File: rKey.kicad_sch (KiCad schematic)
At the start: 39 parts, among them IC1 BDX34C, J1 Conn_01x06, Q1 BC337, Q2 BC337, Q3 BC337, Q4 BC337, Q5 BC327, Q8 BC337, U1 TL084BCN, U2 LM7810_TO220

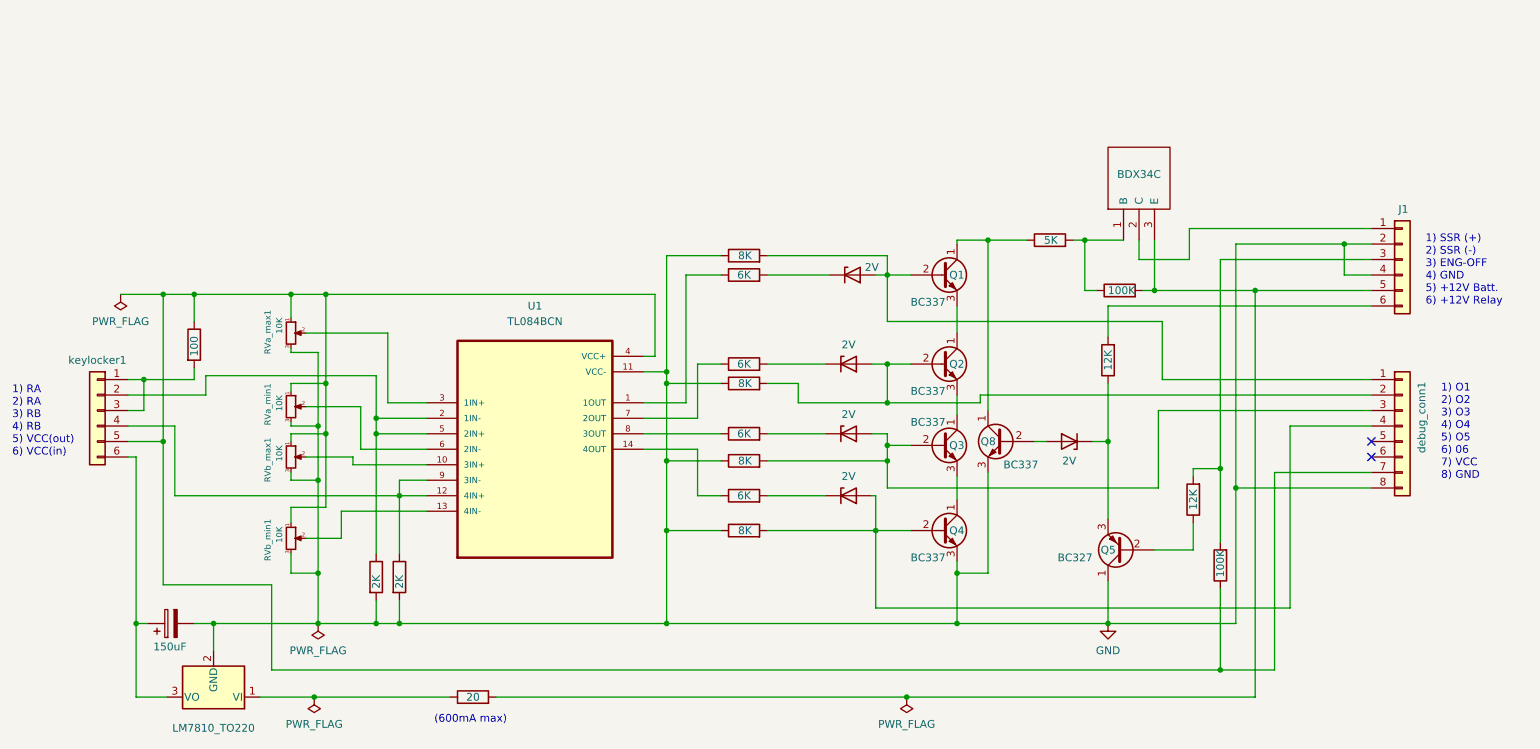
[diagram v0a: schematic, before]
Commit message: Release based on two D45VH10 (10A --> 3W) 2.5% wasted power
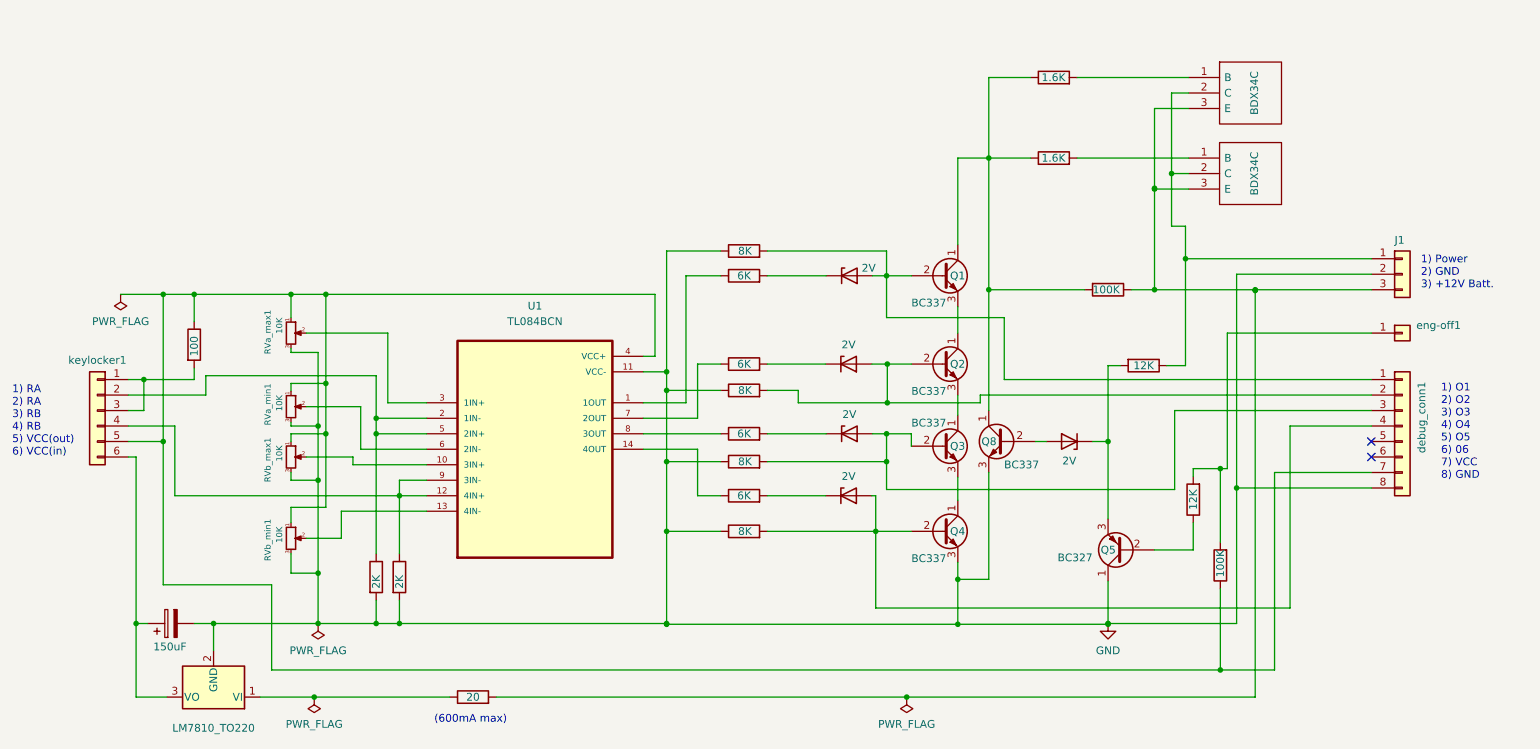
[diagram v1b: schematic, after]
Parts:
- removed J1: Conn_01x06, Connector_Wire:SolderWire-0.5sqmm_1x06_P4.6mm_D0.9mm_OD2.1mm, symbol Connector_Generic:Conn_01x06
- added IC2: BDX34C, BDX34C:TO270P460X1020X2008-3P, symbol BDX34C:BDX34C
- added J1: Conn_01x03, Connector_Wire:SolderWire-1sqmm_1x03_P5.4mm_D1.4mm_OD2.7mm, symbol Connector_Generic:Conn_01x03
- added R18: 1.6K, Resistor_THT:R_Axial_DIN0207_L6.3mm_D2.5mm_P10.16mm_Horizontal, symbol Device:R
- added eng-off1: Conn_01x01, Connector_Wire:SolderWire-0.5sqmm_1x01_D0.9mm_OD2.1mm, symbol Connector_Generic:Conn_01x01
- R10: value 5K -> 1.6K
- R11, R13, R14, R2, R3, R4, R5, R7, R8, R9: footprint Resistor_THT:R_Axial_DIN0207_L6.3mm_D2.5mm_P10.16mm_Horizontal -> Resistor_THT:R_Axial_DIN0204_L3.6mm_D1.6mm_P7.62mm_Horizontal
- ZD1, ZD2, ZD3, ZD4, ZD5: footprint Diode_THT:D_DO-34_SOD68_P10.16mm_Horizontal -> Diode_THT:D_DO-34_SOD68_P7.62mm_Horizontal
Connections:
- net GND: now also J1.2 (Pin_2)
- net at Q5.3 (E), ZD1.1 (K): now also R9.2; no longer R9.1
- net at R13.2, R14.2: now also eng-off1.1 (Pin_1)
- net at IC1.1 (B), R10.2: no longer R11.1
- net at IC1.3 (E), R6.2: now also R11.1, IC2.3 (E), J1.3 (Pin_3); no longer R11.2
- net at Q1.1 (C), Q8.1 (C), R10.1: now also R11.2, R18.1
- net at IC1.2 (C): now also R9.1, IC2.2 (C), J1.1 (Pin_1)
- new net: IC2.1 (B), R18.2
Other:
- note added: "1) Power 2) GND 3) +12V Batt."
- note removed: "1) SSR (+) 2) SSR (-) 3) ENG-OFF 4) GND 5) +12V Batt. 6) +12V Relay"

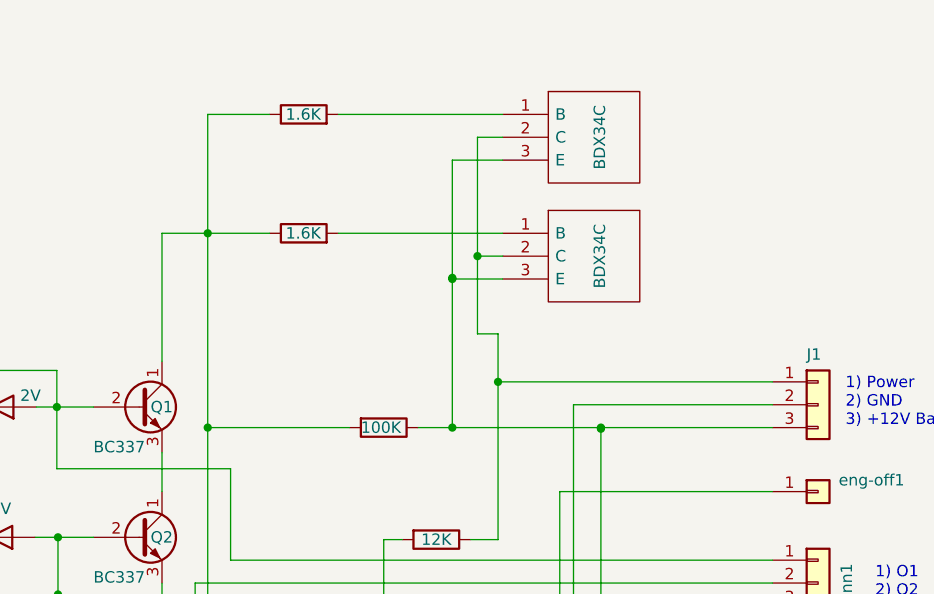
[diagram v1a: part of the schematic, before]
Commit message: Fix: wrong resistors power size
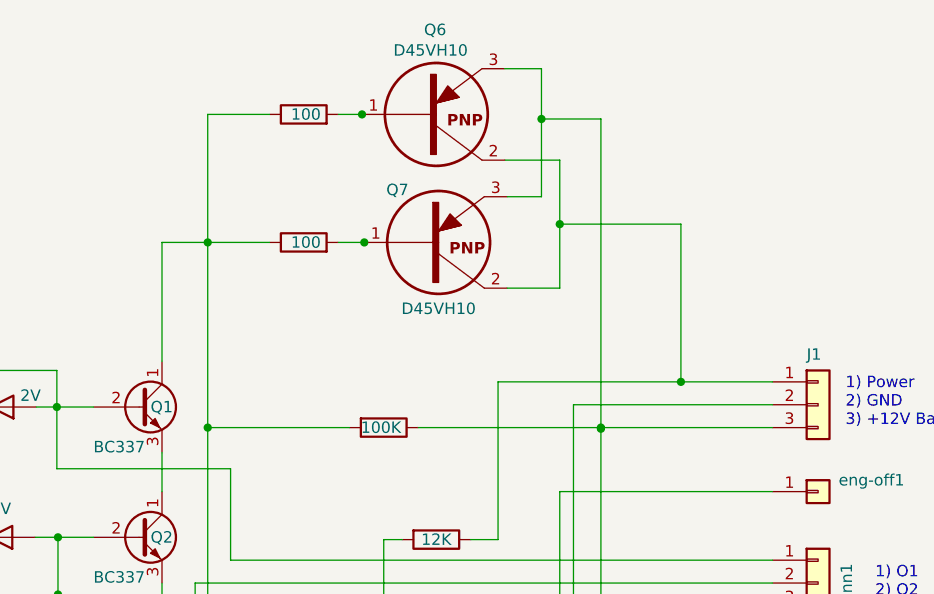
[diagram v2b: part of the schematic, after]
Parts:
- removed IC1, IC2: BDX34C, BDX34C:TO270P460X1020X2008-3P, symbol BDX34C:BDX34C
- added Q6, Q7: D45VH10, Package_TO_SOT_THT:TO-220-3_Vertical, symbol D45VH10:D45VH10
- R10, R18: value 1.6K -> 100; footprint Resistor_THT:R_Axial_DIN0207_L6.3mm_D2.5mm_P10.16mm_Horizontal -> Resistor_THT:R_Axial_DIN0516_L15.5mm_D5.0mm_P20.32mm_Horizontal
- R12, R15, R16, R17: footprint Resistor_THT:R_Axial_DIN0207_L6.3mm_D2.5mm_P10.16mm_Horizontal -> Resistor_THT:R_Axial_DIN0204_L3.6mm_D1.6mm_P7.62mm_Horizontal
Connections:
- net at R18.2: now also Q6.1
- net at J1.1 (Pin_1), R9.1: now also Q6.2, Q7.2
- net at J1.3 (Pin_3), R11.1, R6.2: now also Q6.3, Q7.3
- net at R10.2: now also Q7.1

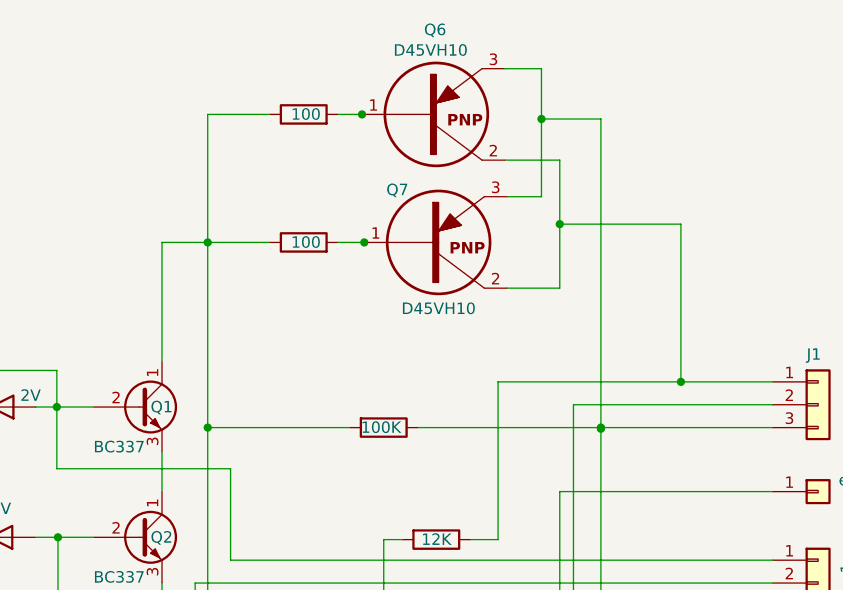
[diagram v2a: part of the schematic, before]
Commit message: fix: porting to the new D45VH10 symbol
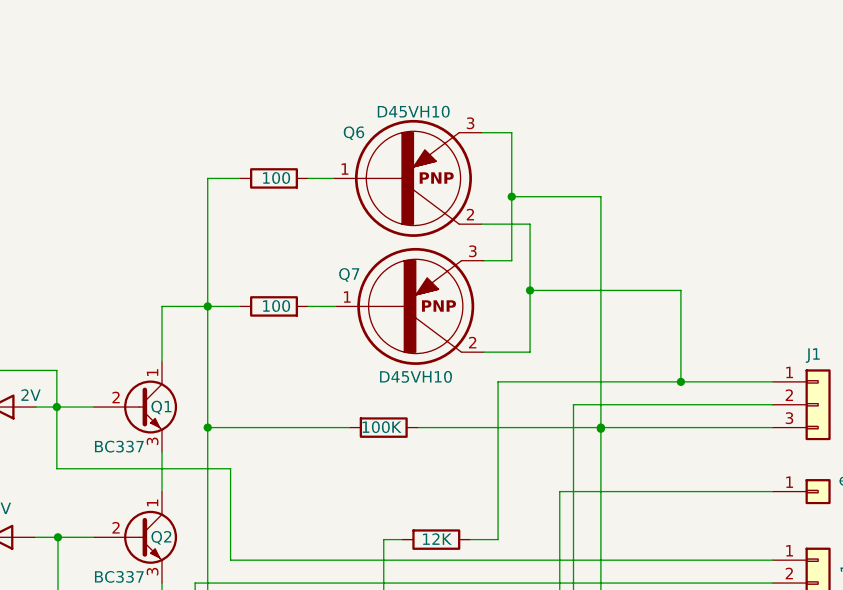
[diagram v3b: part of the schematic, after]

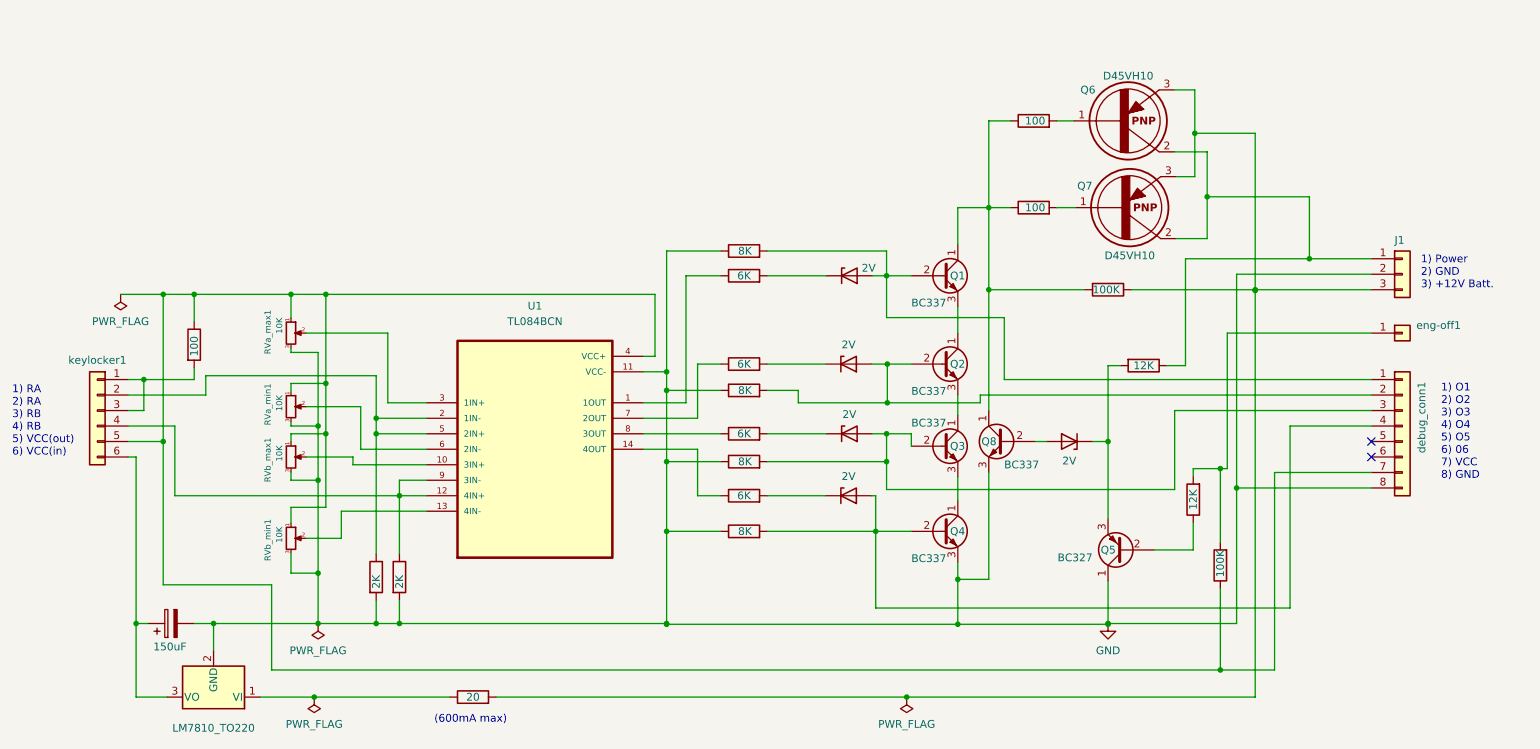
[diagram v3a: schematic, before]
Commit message: Fix: engine locked off when the vehicle is off
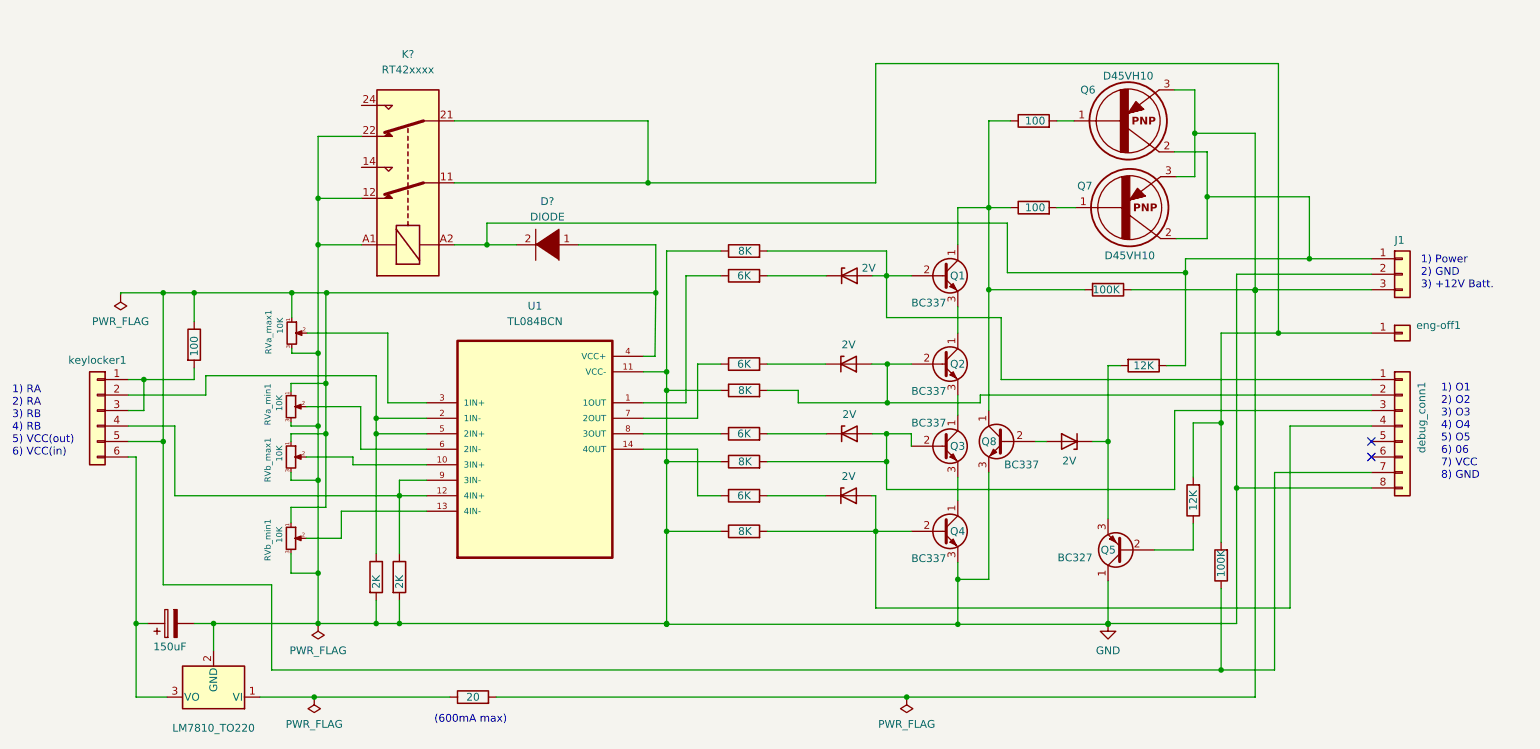
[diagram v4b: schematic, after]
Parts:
- added D?: DIODE, symbol pspice:DIODE
- added K?: RT42xxxx, Relay_THT:Relay_DPDT_Schrack-RT2-FormC_RM5mm, symbol Relay:RT42xxxx
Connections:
- net GND: now also K?.12, K?.22, K?.A1
- net at R13.2, R14.2, eng-off1.1 (Pin_1): now also K?.11, K?.21
- net at J1.1 (Pin_1), Q6.2, Q7.2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: now also D?.2 (A), K?.A2
- net at R1.1, R14.1, RVa_max1.1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: now also D?.1 (K)

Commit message: Feat: Circuit for engine locking when vehicle is off
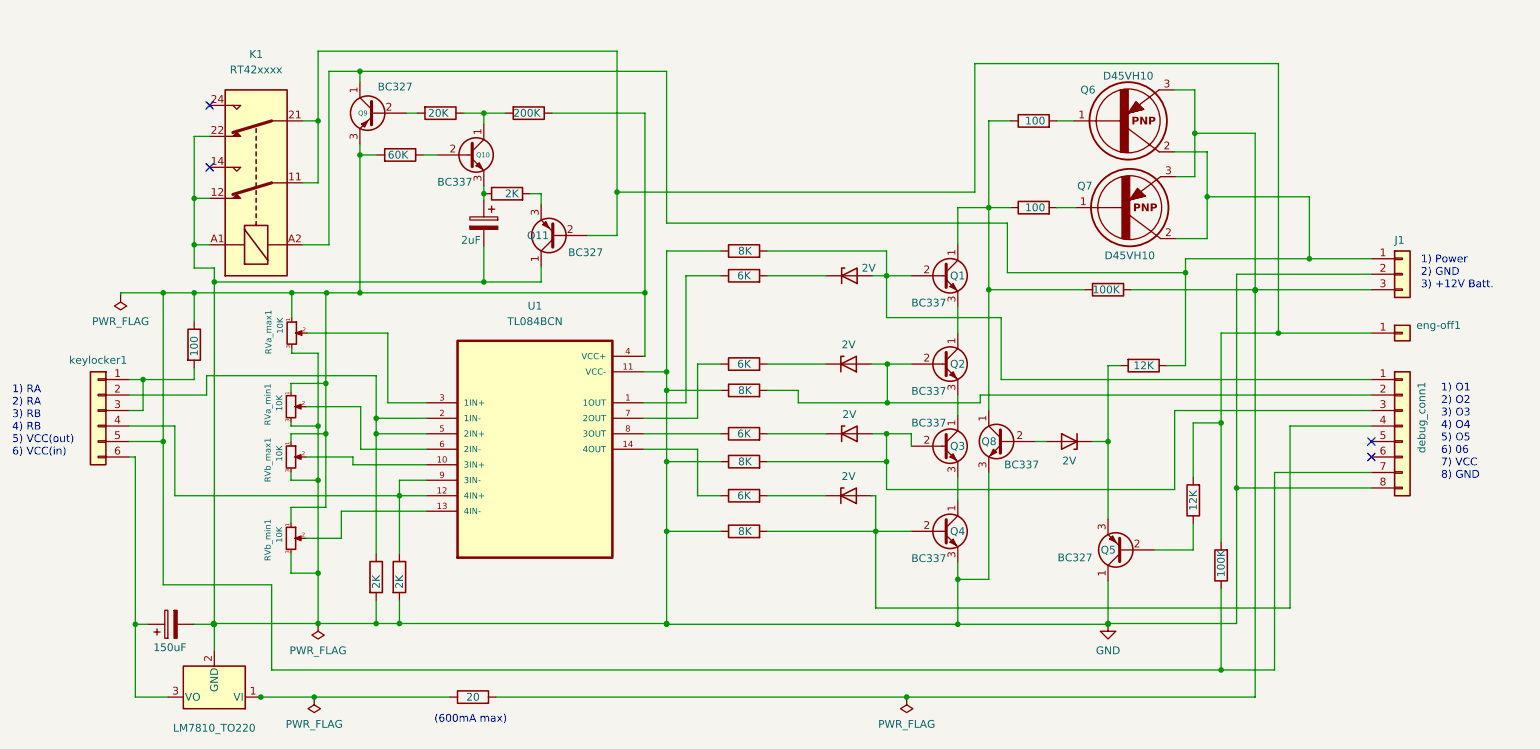
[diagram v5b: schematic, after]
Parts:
- removed D?: DIODE, symbol pspice:DIODE
- added C2: 2uF, Capacitor_THT:CP_Radial_D7.5mm_P2.50mm, symbol Device:C_Polarized
- added Q10: BC337, Package_TO_SOT_THT:TO-92L_Inline_Wide, symbol Transistor_BJT:BC337
- added Q11, Q9: BC327, Package_TO_SOT_THT:TO-92L_Inline_Wide, symbol Transistor_BJT:BC327
- added R19: 60K, Resistor_THT:R_Axial_DIN0204_L3.6mm_D1.6mm_P7.62mm_Horizontal, symbol Device:R
- added R20: 20K, Resistor_THT:R_Axial_DIN0204_L3.6mm_D1.6mm_P7.62mm_Horizontal, symbol Device:R
- added R21: 2K, Resistor_THT:R_Axial_DIN0204_L3.6mm_D1.6mm_P7.62mm_Horizontal, symbol Device:R
- added R22: 200K, Resistor_THT:R_Axial_DIN0204_L3.6mm_D1.6mm_P7.62mm_Horizontal, symbol Device:R
- gave numbers to parts that had none: 1
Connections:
- net GND: now also C2.2, Q11.1 (C)
- net at K1.11, K1.21, R13.2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: now also Q11.2 (B)
- net at J1.1 (Pin_1), K1.A2, Q6.2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: now also Q9.1 (C)
- net at R1.1, R14.1, RVa_max1.1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: now also Q9.3 (E), R19.2, R22.1
- new net: C2.1, Q10.3 (E), R21.1
- new net: Q11.3 (E), R21.2
- new net: Q10.1 (C), R20.1, R22.2
- new net: Q10.2 (B), R19.1
- new net: Q9.2 (B), R20.2
- no-connect marks 2 -> 4
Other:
- moved on the sheet: K1
